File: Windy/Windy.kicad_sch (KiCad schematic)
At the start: 10 parts, among them IC1 MPXV7007DP, IC2 MPXV7007DP

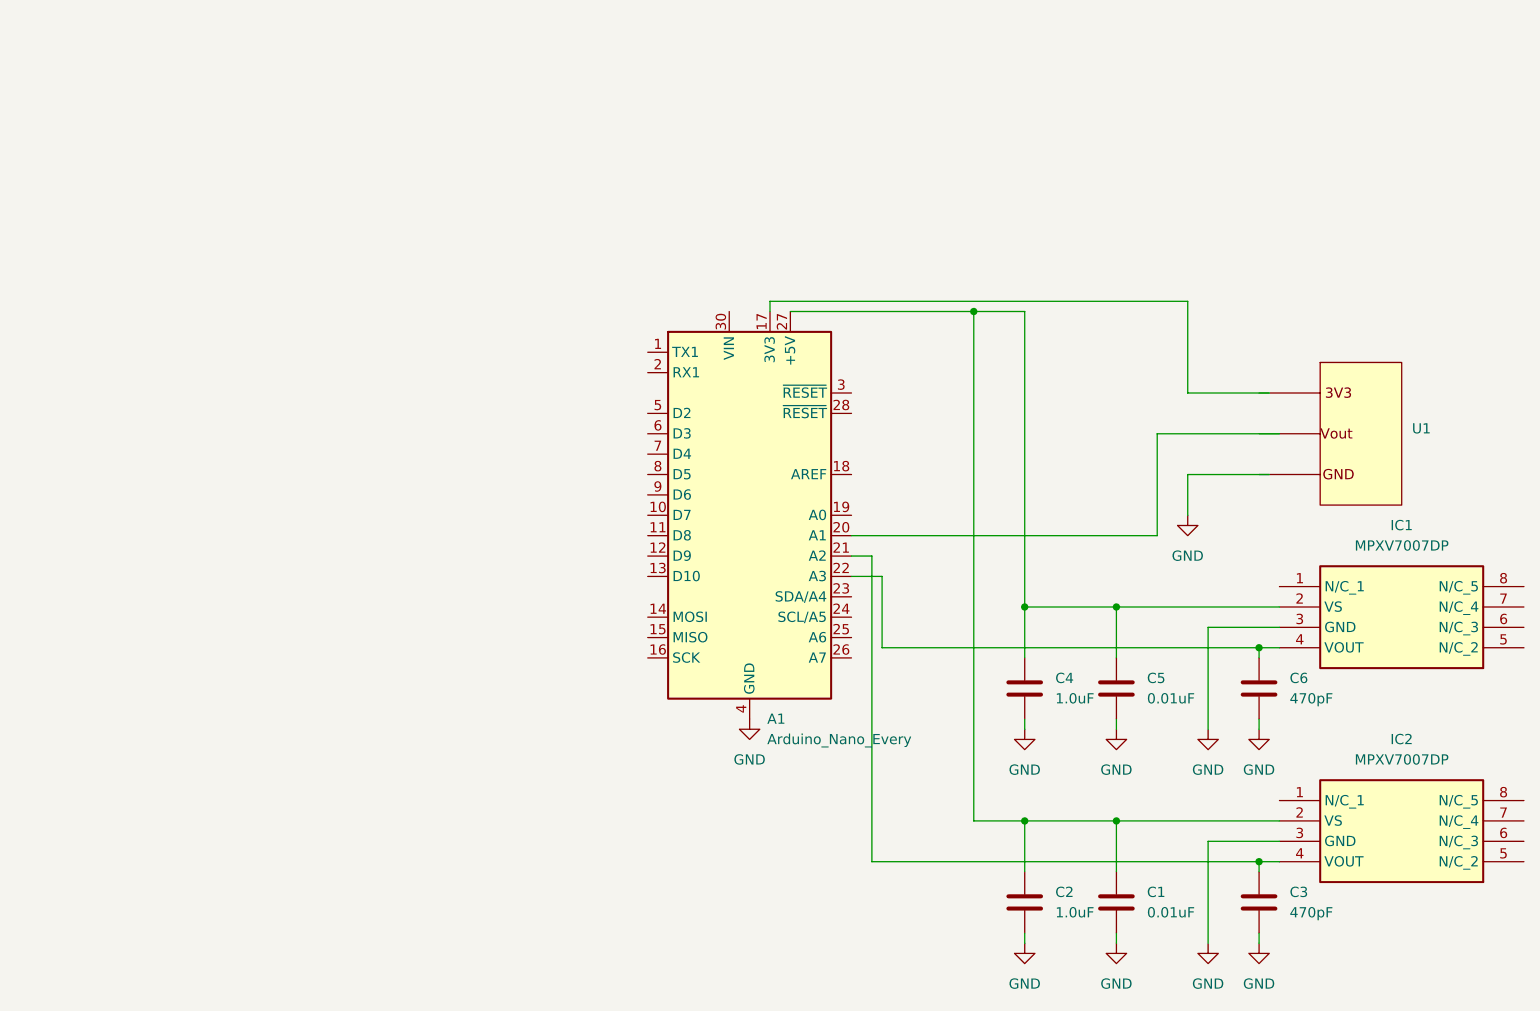
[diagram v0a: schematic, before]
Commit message: Added HC05, RTC Module, SD card reader
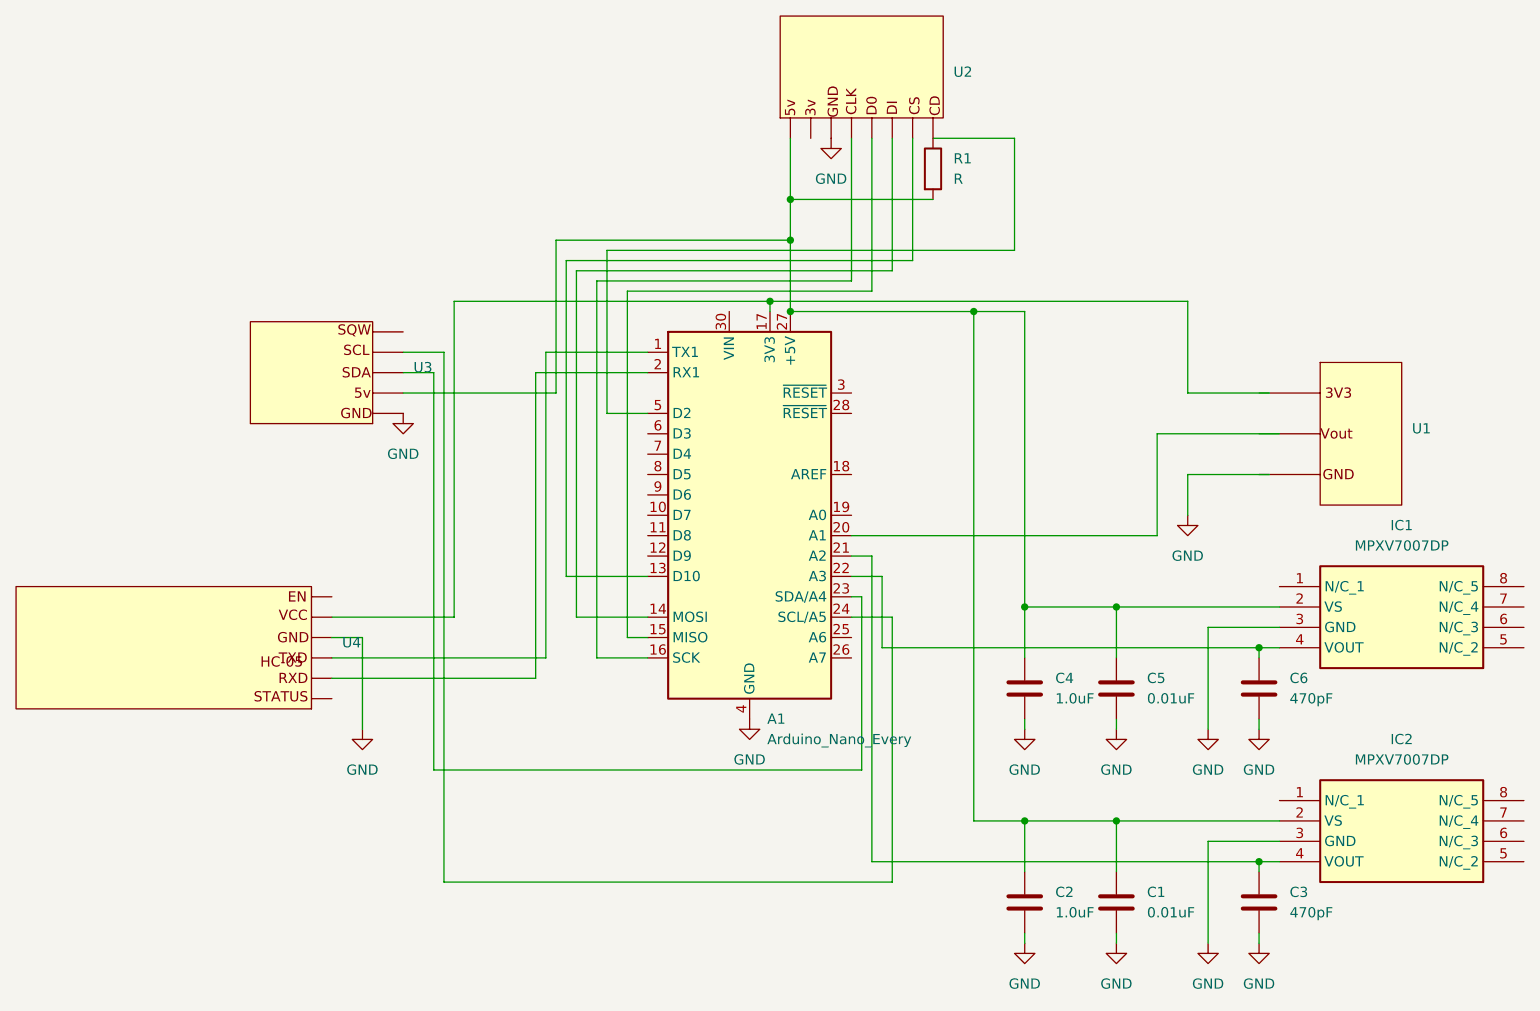
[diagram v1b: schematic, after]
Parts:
- added R1: R, symbol Device:R
- added U2: ~, symbol Windy_Components:MicroSD_card_breakout_board+
- added U3: ~, symbol Windy_Components:RTC_Module
- added U4: ~, symbol Windy_Components:HC05
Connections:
- net at A1.27 (+5V), C1.1, C2.1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: now also R1.2
- net at A1.5 (D2): now also R1.1
